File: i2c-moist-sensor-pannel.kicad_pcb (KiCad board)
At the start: 2 copper layers, 100 x 150 mm, 154 parts, among them IC1 ATTINY441-SSU, P1 CONN_02X03, X1 16MHz

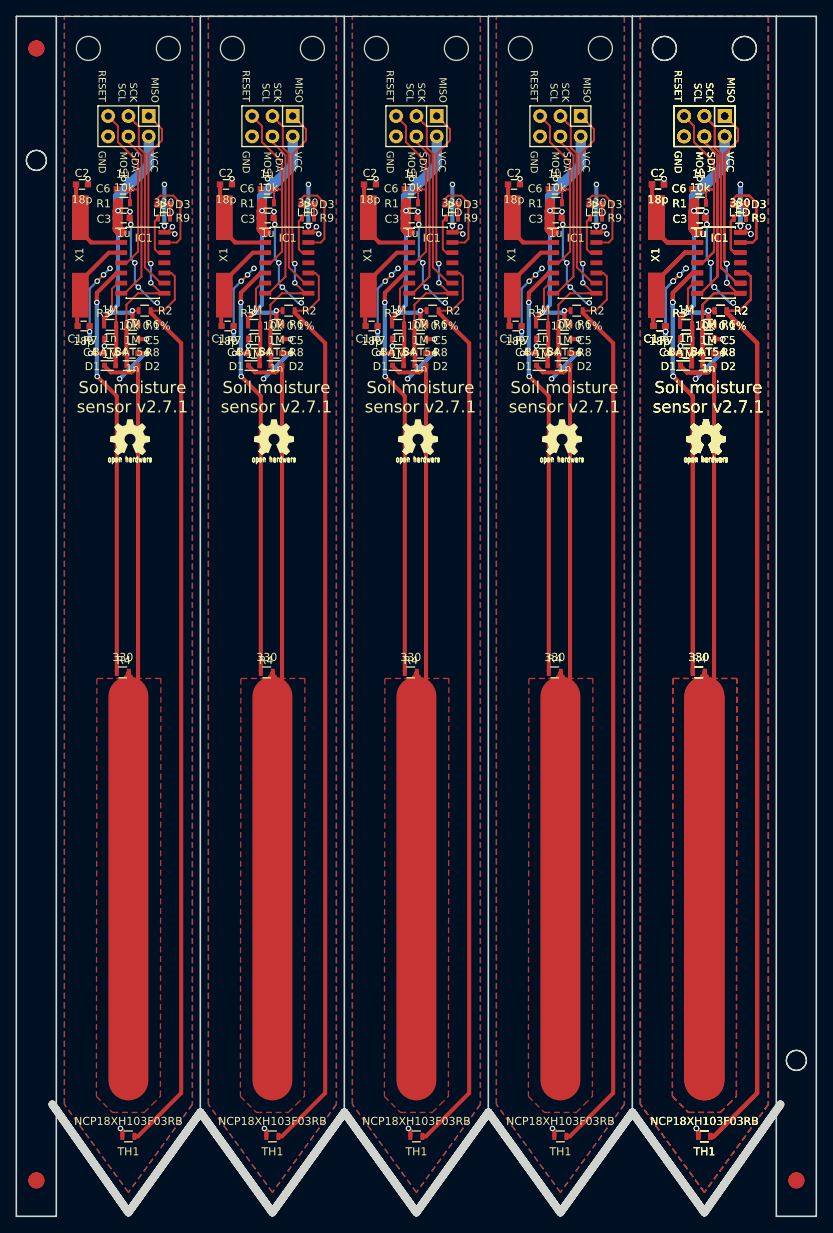
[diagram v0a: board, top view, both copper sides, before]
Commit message: Put the new version to the pannel
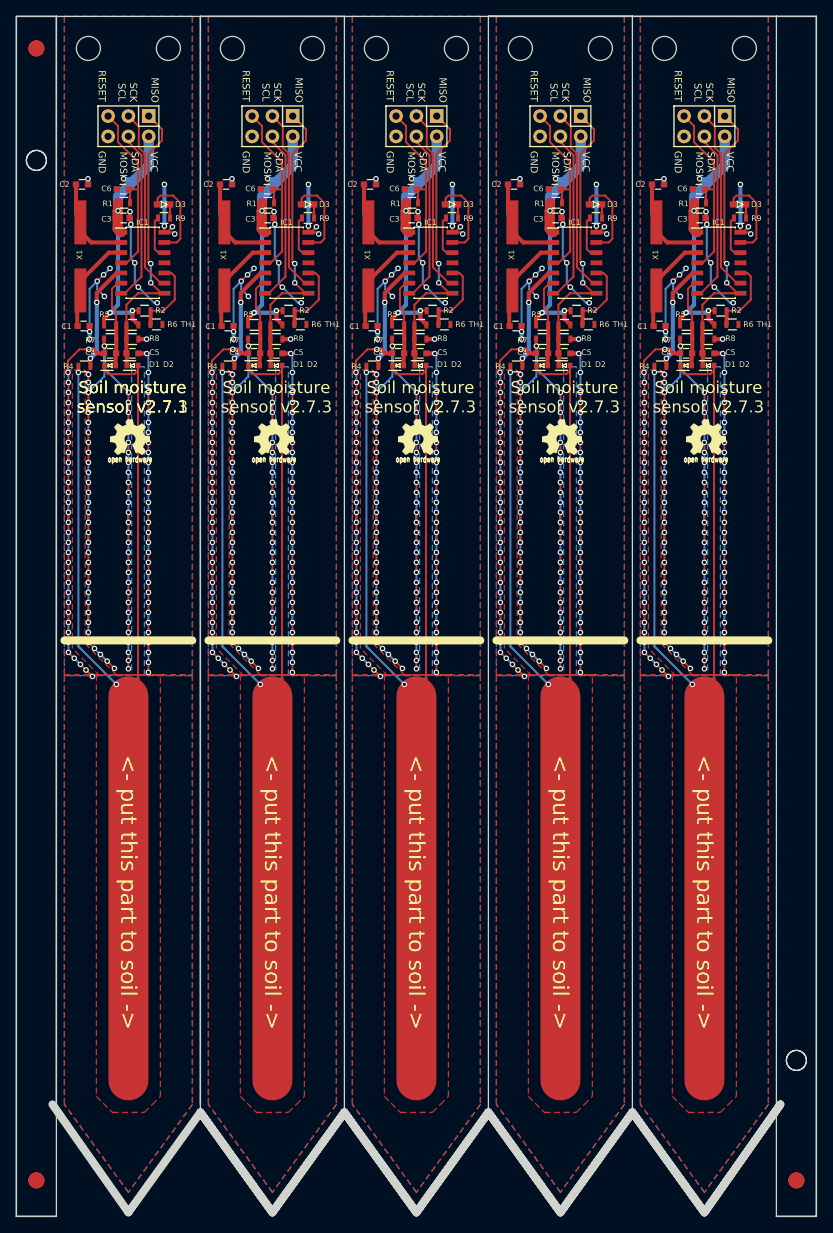
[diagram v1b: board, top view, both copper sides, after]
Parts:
- removed the C1 at (160.4, 60.7) (x2)
- removed the C2 at (160.2, 43.0) (x2)
- removed the C3 at (165.4, 47.2) (x2)
- removed the C4 at (163.7, 64.1) (x2)
- removed the C5 at (166.5, 64.1) (x2)
- removed the C6 at (165.3, 43.6) (x2)
- removed the D1 at (163.7, 65.6) (x2)
- removed the D2 at (166.5, 65.6) (x2)
- removed the D3 at (170.4, 45.5) (x2)
- removed the G*** at (166.2, 74.6) (x2)
- removed the IC1 at (167.8, 52.8) (x2)
- removed the P1 at (166.0, 35.7) (x2)
- removed the R1 at (165.4, 45.3) (x2)
- removed the R2 at (168.0, 58.8) (x2)
- removed the R4 at (165.3, 104.0) (x2)
- removed the R4 at (147.3, 104.0)
- removed the R4 at (111.3, 104.0)
- removed the R4 at (93.3, 104.0)
- removed the R4 at (129.3, 104.0)
- removed the R5 at (163.7, 60.6) (x2)
- removed the R6 at (166.5, 60.6) (x2)
- removed the R7 at (163.7, 62.3) (x2)
- removed the R8 at (166.5, 62.3) (x2)
- removed the R9 at (170.4, 47.2) (x2)
- removed the REF** at (177.5, 167.5) (x2)
- removed the REF** at (82.5, 26.0) (x2)
- removed the REF** at (177.5, 152.5) (x2)
- removed the REF** at (82.5, 40.0) (x2)
- removed the REF** at (161.0, 26.0) (x2)
- removed the REF** at (171.0, 26.0) (x2)
- removed the REF** at (82.5, 167.5) (x2)
- removed the TH1 at (166.0, 162.0) (x2)
- removed the TH1 at (148.0, 162.0)
- removed the TH1 at (112.0, 162.0)
- removed the TH1 at (94.0, 162.0)
- removed the TH1 at (130.0, 162.0)
- removed the X1 at (160.0, 52.0) (x2)
- added C1: 18p, Capacitors_SMD:C_0603, F.Cu at (160.4, 60.7)
- added C2: 18p, Capacitors_SMD:C_0603, F.Cu at (160.2, 43.0)
- added C3: 1u, Capacitors_SMD:C_0603, F.Cu at (165.4, 47.2)
- added C4: 1n, Capacitors_SMD:C_0603, F.Cu at (163.7, 64.1)
- added C5: 1n, Capacitors_SMD:C_0603, F.Cu at (166.5, 64.1)
- added C6: 1u, Capacitors_SMD:C_0603, F.Cu at (165.3, 43.6)
- added D1: BAT54, SMD_Packages:SOD-523, F.Cu at (163.7, 65.6)
- added D2: BAT54, SMD_Packages:SOD-523, F.Cu at (166.5, 65.6)
- added D3: LED, LEDs:LED-0603, F.Cu at (170.4, 45.5)
- added G***: LOGO, chirp_logo:ziogas, F.Cu at (166.5, 46.0)
- added G***: LOGO, chirp_logo:ziogas, F.Cu at (94.5, 46.0)
- added G***: LOGO, chirp_logo:ziogas, F.Cu at (112.5, 46.0)
- added G***: LOGO, chirp_logo:ziogas, F.Cu at (130.5, 46.0)
- added G***: LOGO, chirp_logo:ziogas, F.Cu at (148.5, 46.0)
- added G***: LOGO, w_logo:Logo_silk_OSHW_6x6mm, F.Cu at (166.2, 74.6)
- added IC1: ATTINY441-SSU, Housings_SOIC:SOIC-14_3.9x8.7mm_Pitch1.27mm, F.Cu at (167.8, 52.8)
- added P1: CONN_02X03, Pin_Headers:Pin_Header_Straight_2x03, F.Cu at (166.0, 35.7)
- added R1: 10k, Resistors_SMD:R_0603, F.Cu at (165.4, 45.3)
- added R2: 10k 0.1%, Resistors_SMD:R_0603, F.Cu at (168.0, 58.8)
- added R4: 330, Resistors_SMD:R_0603, F.Cu at (88.5, 65.8)
- added R4: 330, Resistors_SMD:R_0603, F.Cu at (106.5, 65.8)
- added R4: 330, Resistors_SMD:R_0603, F.Cu at (124.5, 65.8)
- added R4: 330, Resistors_SMD:R_0603, F.Cu at (142.5, 65.8)
- added R4: 330, Resistors_SMD:R_0603, F.Cu at (160.5, 65.8)
- added R5: 1M, Resistors_SMD:R_0603, F.Cu at (163.7, 60.6)
- added R6: 1M, Resistors_SMD:R_0603, F.Cu at (166.5, 60.6)
- added R7: 1M, Resistors_SMD:R_0603, F.Cu at (163.7, 62.3)
- added R8: 1M, Resistors_SMD:R_0603, F.Cu at (166.5, 62.3)
- added R9: 330, Resistors_SMD:R_0603, F.Cu at (170.4, 47.2)
- added REF** (x2): Fiducial_Modern_CopperTop, Fiducials:Fiducial_Modern_CopperTop, F.Cu at (177.5, 167.5)
- added REF** (x2): MountingHole_2-5mm, Mounting_Holes:MountingHole_2-5mm, F.Cu at (82.5, 40.0)
- added REF**: MountingHole_3mm, Mounting_Holes:MountingHole_3mm, F.Cu at (161.0, 26.0)
- added REF** (x2): Fiducial_Modern_CopperTop, Fiducials:Fiducial_Modern_CopperTop, F.Cu at (82.5, 167.5)
- added REF**: MountingHole_3mm, Mounting_Holes:MountingHole_3mm, F.Cu at (171.0, 26.0)
- added REF** (x2): Fiducial_Modern_CopperTop, Fiducials:Fiducial_Modern_CopperTop, F.Cu at (82.5, 26.0)
- added REF** (x2): MountingHole_2-5mm, Mounting_Holes:MountingHole_2-5mm, F.Cu at (177.5, 152.5)
- added TH1: NCP18XH103F03RB, Resistors_SMD:R_0603, F.Cu at (97.5, 60.5)
- added TH1: NCP18XH103F03RB, Resistors_SMD:R_0603, F.Cu at (115.5, 60.5)
- added TH1: NCP18XH103F03RB, Resistors_SMD:R_0603, F.Cu at (133.5, 60.5)
- added TH1: NCP18XH103F03RB, Resistors_SMD:R_0603, F.Cu at (151.5, 60.5)
- added TH1: NCP18XH103F03RB, Resistors_SMD:R_0603, F.Cu at (169.5, 60.5)
- added X1: 16MHz, Crystals:Crystal_HC49-SD_SMD, F.Cu at (160.0, 52.0)
- turned D3 to 270 degrees (x4)
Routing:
- net GND: track 261.4 -> 1118.3 mm, vias 126 -> 720
- net /THERMISTOR: track 692.6 -> 48.5 mm
- net /EXCITATION: track 315.3 -> 68.0 mm, vias 12 -> 10
- net /SENSOR_TRACK: track 591.9 -> 704.1 mm, vias 0 -> 10
- net /MISO/SENSE_HIGH: track 228.7 -> 190.6 mm, vias 12 -> 10
- net VCC: track 223.3 -> 186.1 mm, vias 24 -> 20
- net /RESET: track 144.5 -> 120.4 mm
- net /SCK/SCL: track 138.0 -> 115.0 mm
- net /MOSI/SDA: track 130.4 -> 108.6 mm
- net Net-(C1-Pad1): track 73.8 -> 61.5 mm
- net Net-(C2-Pad1): track 71.3 -> 59.4 mm
- net /SENSE_LOW: track 69.2 -> 57.7 mm
- net Net-(D3-Pad1): track 64.8 -> 54.0 mm
- net Net-(IC1-Pad12): track 32.7 -> 27.2 mm
- net Net-(D3-Pad2): track 10.3 -> 8.61 mm
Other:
- outline, holes or cut-outs redrawn
- net class excitation added: clearance 0.6, trace_width 0.254, via_dia 0.7, via_drill 0.4
- board text added: "<- put this part to soil ->"
- board text added: "Soil moisture sensor v2.7.3"

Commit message: Remove sharp corners so that heatshrink lays nicer
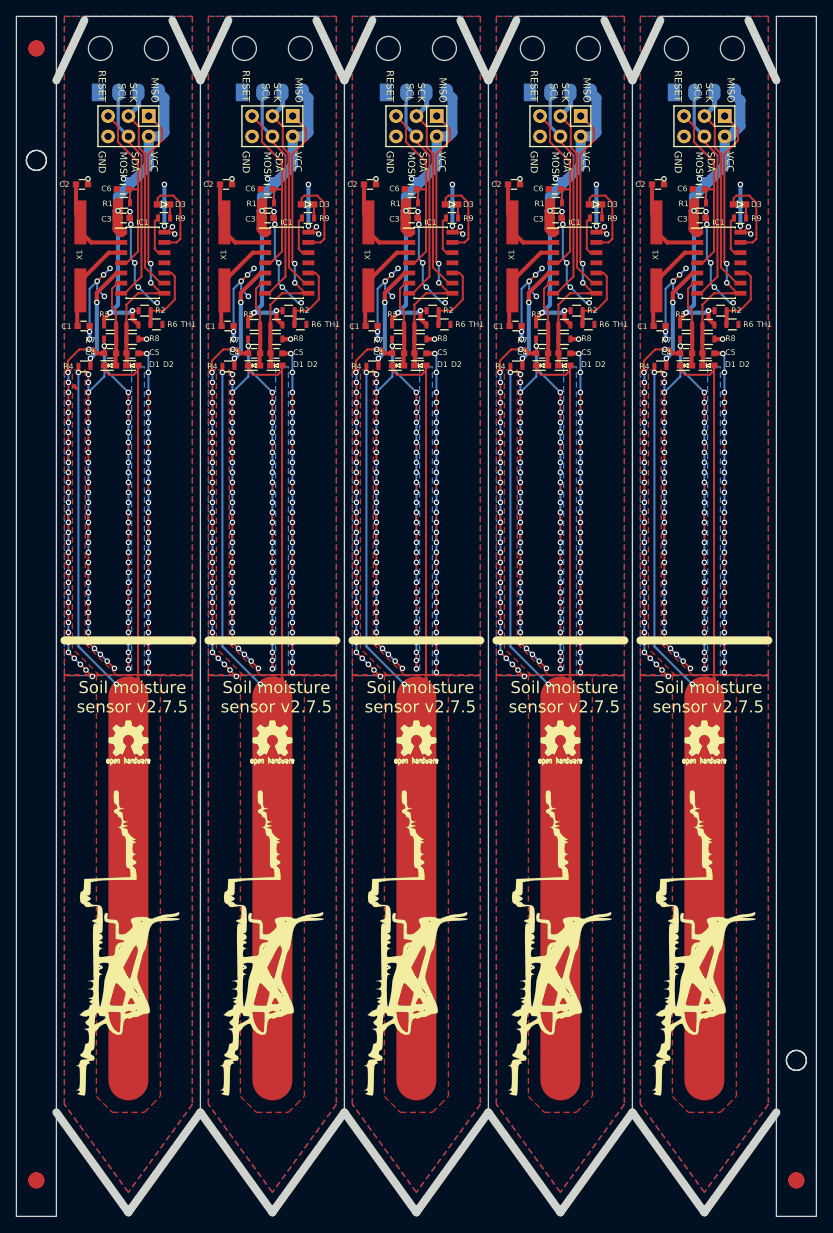
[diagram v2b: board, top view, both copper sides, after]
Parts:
- removed the G*** at (94.2, 74.6)
- removed the G*** at (166.5, 46.0)
- removed the G*** at (94.5, 46.0)
- removed the G*** at (112.2, 74.6)
- removed the G*** at (112.5, 46.0)
- removed the G*** at (130.2, 74.6)
- removed the G*** at (130.5, 46.0)
- removed the G*** at (148.2, 74.6)
- removed the G*** at (148.5, 46.0)
- removed the G*** at (166.2, 74.6)
- removed the REF** at (177.5, 167.5) (x2)
- removed the REF** at (82.5, 40.0) (x2)
- removed the REF** at (89.0, 26.0)
- removed the REF** at (99.0, 26.0)
- removed the REF** at (107.0, 26.0)
- removed the REF** at (117.0, 26.0)
- removed the REF** at (125.0, 26.0)
- removed the REF** at (135.0, 26.0)
- removed the REF** at (143.0, 26.0)
- removed the REF** at (153.0, 26.0)
- removed the REF** at (161.0, 26.0)
- removed the REF** at (82.5, 167.5) (x2)
- removed the REF** at (171.0, 26.0)
- removed the REF** at (82.5, 26.0) (x2)
- removed the REF** at (177.5, 152.5) (x2)
- added G***: LOGO, w_logo:Logo_silk_OSHW_6x6mm, F.Cu at (94.0, 112.2)
- added G***: LOGO, chirp_logo:ziogas, B.Cu at (166.0, 137.8)
- added G***: LOGO, chirp_logo:ziogas, B.Cu at (94.0, 137.8)
- added G***: LOGO, w_logo:Logo_silk_OSHW_6x6mm, F.Cu at (112.0, 112.2)
- added G***: LOGO, chirp_logo:ziogas, B.Cu at (112.0, 137.8)
- added G***: LOGO, w_logo:Logo_silk_OSHW_6x6mm, F.Cu at (130.0, 112.2)
- added G***: LOGO, chirp_logo:ziogas, B.Cu at (130.0, 137.8)
- added G***: LOGO, w_logo:Logo_silk_OSHW_6x6mm, F.Cu at (148.0, 112.2)
- added G***: LOGO, chirp_logo:ziogas, B.Cu at (148.0, 137.8)
- added G***: LOGO, w_logo:Logo_silk_OSHW_6x6mm, F.Cu at (166.0, 112.2)
- added PIN_SOCKET_4: Val**, w_pin_strip:pin_socket_4, B.Cu at (94.0, 31.5)
- added PIN_SOCKET_4: Val**, w_pin_strip:pin_socket_4, B.Cu at (112.0, 31.5)
- added PIN_SOCKET_4: Val**, w_pin_strip:pin_socket_4, B.Cu at (130.0, 31.5)
- added PIN_SOCKET_4: Val**, w_pin_strip:pin_socket_4, B.Cu at (148.0, 31.5)
- added PIN_SOCKET_4: Val**, w_pin_strip:pin_socket_4, B.Cu at (166.0, 31.5)
- added REF** (x2): Fiducial_Modern_CopperTop, Fiducials:Fiducial_Modern_CopperTop, F.Cu at (177.5, 167.5)
- added REF** (x2): MountingHole_2-5mm, Mounting_Holes:MountingHole_2-5mm, F.Cu at (82.5, 40.0)
- added REF**: MountingHole_3mm, Mounting_Holes:MountingHole_3mm, F.Cu at (90.5, 26.0)
- added REF**: MountingHole_3mm, Mounting_Holes:MountingHole_3mm, F.Cu at (97.5, 26.0)
- added REF**: MountingHole_3mm, Mounting_Holes:MountingHole_3mm, F.Cu at (108.5, 26.0)
- added REF**: MountingHole_3mm, Mounting_Holes:MountingHole_3mm, F.Cu at (115.5, 26.0)
- added REF**: MountingHole_3mm, Mounting_Holes:MountingHole_3mm, F.Cu at (126.5, 26.0)
- added REF**: MountingHole_3mm, Mounting_Holes:MountingHole_3mm, F.Cu at (133.5, 26.0)
- added REF**: MountingHole_3mm, Mounting_Holes:MountingHole_3mm, F.Cu at (144.5, 26.0)
- added REF**: MountingHole_3mm, Mounting_Holes:MountingHole_3mm, F.Cu at (151.5, 26.0)
- added REF**: MountingHole_3mm, Mounting_Holes:MountingHole_3mm, F.Cu at (162.5, 26.0)
- added REF** (x2): Fiducial_Modern_CopperTop, Fiducials:Fiducial_Modern_CopperTop, F.Cu at (82.5, 167.5)
- added REF**: MountingHole_3mm, Mounting_Holes:MountingHole_3mm, F.Cu at (169.5, 26.0)
- added REF** (x2): Fiducial_Modern_CopperTop, Fiducials:Fiducial_Modern_CopperTop, F.Cu at (82.5, 26.0)
- added REF** (x2): MountingHole_2-5mm, Mounting_Holes:MountingHole_2-5mm, F.Cu at (177.5, 152.5)
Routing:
- net VCC: track 186.1 -> 222.9 mm
- net /MOSI/SDA: track 108.6 -> 138.8 mm
- net /SCK/SCL: track 115.0 -> 132.5 mm
- net /SENSOR_TRACK: track 704.1 -> 701.6 mm
- net (no net): track 0.00 -> 0.51 mm
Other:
- outline, holes or cut-outs redrawn
- board text added: "SCL"
- board text added: "SDA"
- board text added: "Soil moisture sensor v2.7.5"
- board text removed: "<- put this part to soil ->"
- board text removed: "Soil moisture sensor v2.7.1"
- board text removed: "Soil moisture sensor v2.7.3"

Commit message: Changes for the next release - stronger vias connecting to the sensor pad, align caps for better coating convenience, use silkscreen as cover for problematic vias
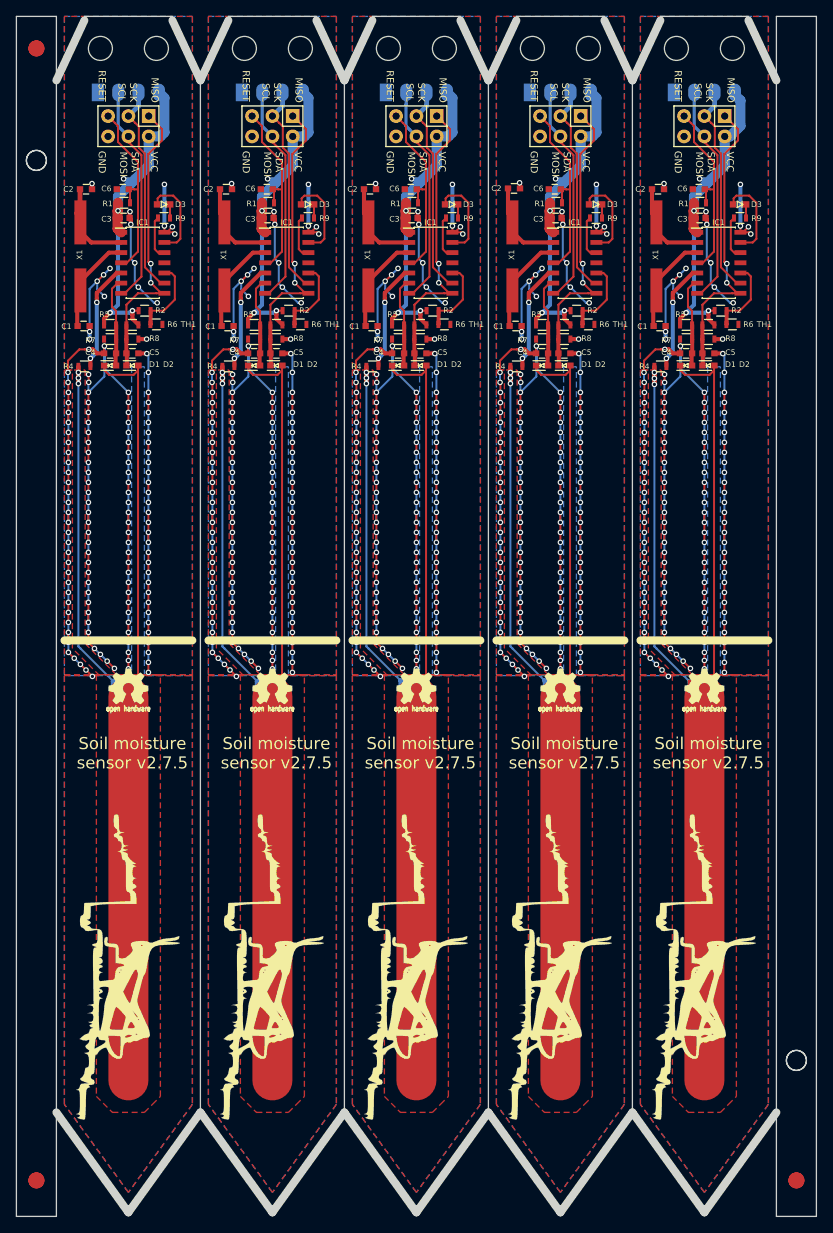
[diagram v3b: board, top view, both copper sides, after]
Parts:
- removed the C2 at (88.2, 43.0)
- removed the C2 at (106.2, 43.0)
- removed the C2 at (124.2, 43.0)
- removed the C2 at (142.2, 43.0)
- removed the C2 at (160.2, 43.0)
- removed the G*** at (94.0, 112.2)
- removed the G*** at (166.0, 137.8)
- removed the G*** at (94.0, 137.8)
- removed the G*** at (112.0, 112.2)
- removed the G*** at (112.0, 137.8)
- removed the G*** at (130.0, 112.2)
- removed the G*** at (130.0, 137.8)
- removed the G*** at (148.0, 112.2)
- removed the G*** at (148.0, 137.8)
- removed the G*** at (166.0, 112.2)
- removed the REF** at (177.5, 167.5) (x2)
- removed the REF** at (82.5, 40.0) (x2)
- removed the REF** at (82.5, 167.5) (x2)
- removed the REF** at (82.5, 26.0) (x2)
- removed the REF** at (177.5, 152.5) (x2)
- added C2: 18p, Capacitors_SMD:C_0603, F.Cu at (88.7, 43.6)
- added C2: 18p, Capacitors_SMD:C_0603, F.Cu at (106.2, 43.6)
- added C2: 18p, Capacitors_SMD:C_0603, F.Cu at (124.2, 43.6)
- added C2: 18p, Capacitors_SMD:C_0603, F.Cu at (142.2, 43.5)
- added C2: 18p, Capacitors_SMD:C_0603, F.Cu at (160.2, 43.6)
- added G***: LOGO, w_logo:Logo_silk_OSHW_6x6mm, F.Cu at (94.0, 105.8)
- added G***: LOGO, chirp_logo:ziogas, B.Cu at (166.0, 140.8)
- added G***: LOGO, chirp_logo:ziogas, B.Cu at (94.0, 140.8)
- added G***: LOGO, w_logo:Logo_silk_OSHW_6x6mm, F.Cu at (112.0, 105.8)
- added G***: LOGO, chirp_logo:ziogas, B.Cu at (112.0, 140.8)
- added G***: LOGO, w_logo:Logo_silk_OSHW_6x6mm, F.Cu at (130.0, 105.8)
- added G***: LOGO, chirp_logo:ziogas, B.Cu at (130.0, 140.8)
- added G***: LOGO, w_logo:Logo_silk_OSHW_6x6mm, F.Cu at (148.0, 105.8)
- added G***: LOGO, chirp_logo:ziogas, B.Cu at (148.0, 140.8)
- added G***: LOGO, w_logo:Logo_silk_OSHW_6x6mm, F.Cu at (166.0, 105.8)
- added REF** (x2): Fiducial_Modern_CopperTop, Fiducials:Fiducial_Modern_CopperTop, F.Cu at (177.5, 167.5)
- added REF** (x2): MountingHole_2-5mm, Mounting_Holes:MountingHole_2-5mm, F.Cu at (82.5, 40.0)
- added REF** (x2): Fiducial_Modern_CopperTop, Fiducials:Fiducial_Modern_CopperTop, F.Cu at (82.5, 167.5)
- added REF** (x2): Fiducial_Modern_CopperTop, Fiducials:Fiducial_Modern_CopperTop, F.Cu at (82.5, 26.0)
- added REF** (x2): MountingHole_2-5mm, Mounting_Holes:MountingHole_2-5mm, F.Cu at (177.5, 152.5)
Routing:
- net /SENSOR_TRACK: track 701.6 -> 750.1 mm, vias 10 -> 30
- net Net-(C2-Pad1): track 59.4 -> 57.7 mm
- net (no net): track 0.51 -> 0.00 mm
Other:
- board text added: "."
